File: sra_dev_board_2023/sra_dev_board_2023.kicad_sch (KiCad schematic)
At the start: 75 parts, among them J1 Conn_01x19_Male, J10 Conn_01x03_Male, J11 Conn_01x05_Male, J12 Conn_01x05_Male, J13 Conn_01x05_Male, J14 Conn_01x03_Male, J15 Conn_01x03_Male, J16 Screw_Terminal_01x05, J17 Conn_01x06_Male, J2 Conn_01x03_Male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

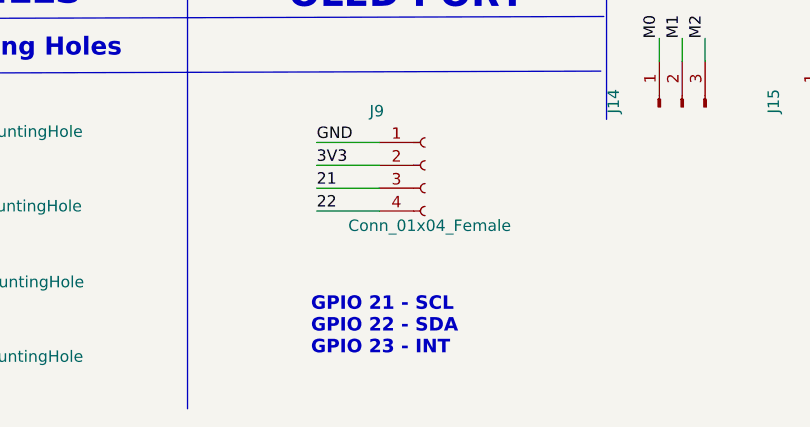
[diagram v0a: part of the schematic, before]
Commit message: Tweaks in routing prototype-1
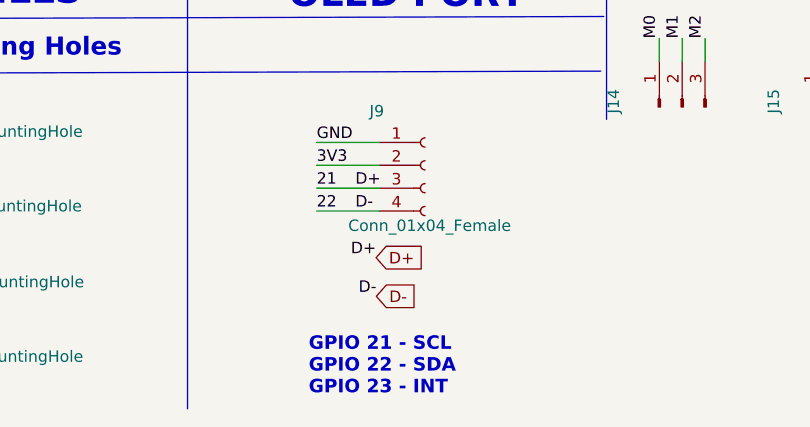
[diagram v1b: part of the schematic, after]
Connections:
- net 21 renamed D+
- net 22 renamed D-
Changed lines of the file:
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@@
     (effects (font (size 3 3) (thickness 0.6) bold) (justify left bottom))
   )
-  (text "GPIO 21 - SCL\nGPIO 22 - SDA\nGPIO 23 - INT\n" (at 144.1704 242.316 0)
+  (text "GPIO 21 - SCL\nGPIO 22 - SDA\nGPIO 23 - INT\n" (at 143.9164 246.761 0)
     (effects (font (size 1.5 1.5) bold) (justify left bottom))
   )
@@
     (effects (font (size 1.27 1.27)) (justify left bottom))
   )
+  (label "D-" (at 151.4348 235.6612 180)
+    (effects (font (size 1.27 1.27)) (justify right bottom))
+  )
   (label "33" (at 26.1366 48.006 0)
     (effects (font (size 1.27 1.27)) (justify left bottom))
@@
     (effects (font (size 1.27 1.27)) (justify right bottom))
   )
+  (label "D+" (at 149.098 223.647 0)
+    (effects (font (size 1.27 1.27)) (justify left bottom))
+  )
   (label "AMS_IN" (at 91.6178 152.908 180)
     (effects (font (size 1.27 1.27)) (justify right bottom))
@@
     (effects (font (size 1.27 1.27)) (justify right bottom))
   )
+  (label "D+" (at 151.4094 231.3686 180)
+    (effects (font (size 1.27 1.27)) (justify right bottom))
+  )
   (label "3V3" (at 200.66 85.09 90)
     (effects (font (size 1.27 1.27)) (justify left bottom))
@@
     (effects (font (size 1.27 1.27)) (justify left bottom))
   )
+  (label "D-" (at 149.098 226.187 0)
+    (effects (font (size 1.27 1.27)) (justify left bottom))
+  )
   (label "3V3" (at 238.76 191.77 0)
     (effects (font (size 1.27 1.27)) (justify left bottom))
@@
     (effects (font (size 1.27 1.27)) (justify left bottom))
   )
+  (global_label "D-" (shape input) (at 151.4348 235.6612 0) (fields_autoplaced)
+    (effects (font (size 1.27 1.27)) (justify left))
+    (property "Intersheet References" "${INTERSHEET_REFS}" (id 0) (at 156.6903 235.5818 0)
+      (effects (font (size 1.27 1.27)) (justify left) hide)
+    )
+  )
+  (global_label "D+" (shape input) (at 151.4094 231.3686 0) (fields_autoplaced)
+    (effects (font (size 1.27 1.27)) (justify left))
+    (property "Intersheet References" "${INTERSHEET_REFS}" (id 0) (at 156.6649 231.2892 0)
+      (effects (font (size 1.27 1.27)) (justify left) hide)
+    )
+  )
   (symbol (lib_id "Device:R") (at 37.8206 175.1838 0) (unit 1)

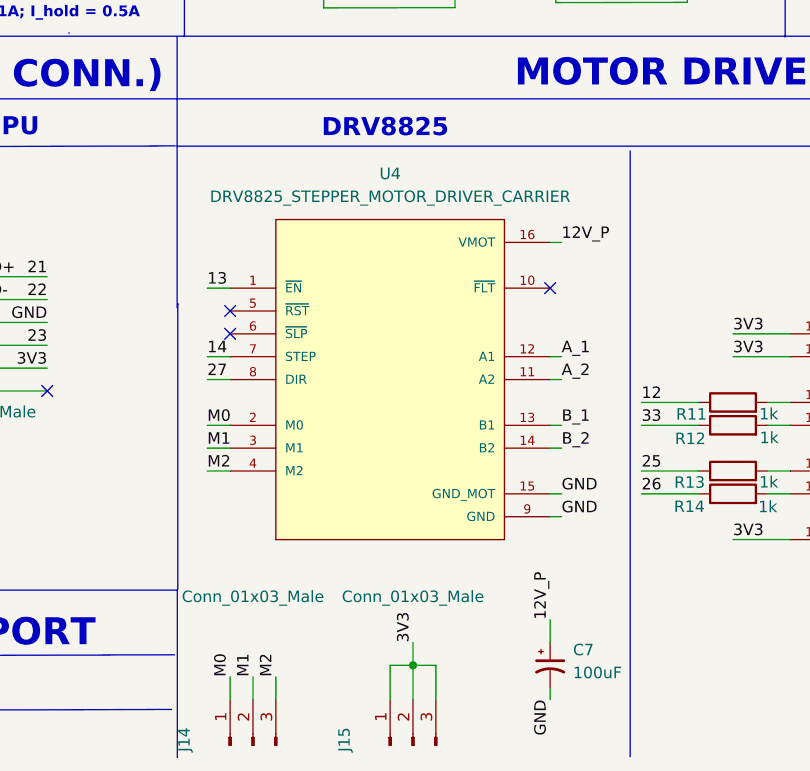
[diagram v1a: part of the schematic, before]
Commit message: Update LSA and SRA board after hardware testing
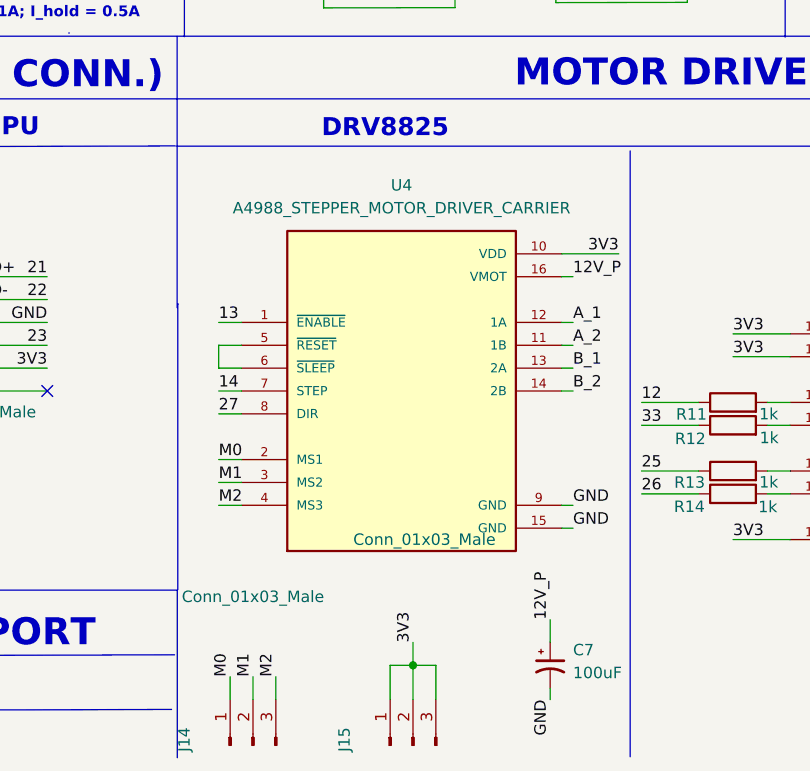
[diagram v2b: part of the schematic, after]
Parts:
- removed U4: DRV8825_STEPPER_MOTOR_DRIVER_CARRIER, stepper_motor_driver:IC_DRV8825_STEPPER_MOTOR_DRIVER_CARRIER, symbol DRV8825_STEPPER_MOTOR_DRIVER_CARRIER:DRV8825_STEPPER_MOTOR_DRIVER_CARRIER
- added U4: A4988_STEPPER_MOTOR_DRIVER_CARRIER, stepper_motor_driver:MODULE_A4988_STEPPER_MOTOR_DRIVER_CARRIER, symbol A4988_STEPPER_MOTOR_DRIVER_CARRIER:A4988_STEPPER_MOTOR_DRIVER_CARRIER
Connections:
- net 12V_P: now also U4.16 (VMOT)
- net 13: now also U4.1 (~{ENABLE})
- net 14: now also U4.7 (STEP)
- net 27: now also U4.8 (DIR)
- net 3V3: now also U4.10 (VDD)
- net A_1: now also U4.12 (1A)
- net A_2: now also U4.11 (1B)
- net B_1: now also U4.13 (2A)
- net B_2: now also U4.14 (2B)
- net GND: now also U4.15 (GND), U4.9 (GND)
- net M0: now also U4.2 (MS1)
- net M1: now also U4.3 (MS2)
- net M2: now also U4.4 (MS3)
- new net: U4.5 (~{RESET}), U4.6 (~{SLEEP})
- no-connect marks 12 -> 9

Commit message: Update repo with recent changes
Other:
- note added: "A4988"
- note removed: "DRV8825"
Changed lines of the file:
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@@
     (effects (font (size 3 3) (thickness 0.6) bold) (justify left bottom))
   )
-  (text "DRV8825" (at 193.04 147.32 0)
+  (text "A4988\n" (at 193.04 147.32 0)
     (effects (font (size 2 2) (thickness 0.6) bold) (justify left bottom))
   )

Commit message: Modify relative path for TCRT5000 footprint
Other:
- note added: "SRA DEVELOPMENT BOARD - 2023"
- note removed: "SRA DEVELOPMENT BOARD - 2022"
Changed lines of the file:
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@@
     (effects (font (size 2 2) (thickness 0.6) bold) (justify left bottom))
   )
-  (text "SRA DEVELOPMENT BOARD - 2022" (at 84.2772 9.8044 0)
+  (text "SRA DEVELOPMENT BOARD - 2023" (at 84.2772 9.8044 0)
     (effects (font (size 5 5) (thickness 1) bold) (justify left bottom))
   )

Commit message: Add current limiting resistor for MPU (#26)
* Add current limiting resistor on Interrupt line for MPU

* Update gerbers, placement files and BoM
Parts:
- added R15: 4.7k, Resistor_SMD:R_0603_1608Metric, symbol Device:R
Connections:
- net 23: now also R15.2; no longer J8.4 (Pin_4)
- new net: J8.4 (Pin_4), R15.1
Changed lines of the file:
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@@
     (stroke (width 0) (type default) (color 0 0 0 0))
   )
+  (wire (pts (xy 173.99 170.18) (xy 170.18 170.18))
+    (stroke (width 0) (type default) (color 0 0 0 0))
+  )
   (wire (pts (xy 151.765 226.187) (xy 144.8054 226.187))
     (stroke (width 0) (type default) (color 0 0 0 0))
@@
     (effects (font (size 1.27 1.27)) (justify left bottom))
   )
-  (label "23" (at 162.56 170.18 180)
+  (label "23" (at 173.99 170.18 180)
     (effects (font (size 1.27 1.27)) (justify right bottom))
   )
@@
     )
   )
+  (symbol (lib_id "Device:R") (at 166.37 170.18 90) (unit 1)
+    (in_bom yes) (on_board yes)
+    (property "Reference" "R15" (id 0) (at 166.37 167.64 90))
+    (property "Value" "4.7k" (id 1) (at 166.37 170.18 90))
+    (property "Footprint" "Resistor_SMD:R_0603_1608Metric" (id 2) (at 166.37 171.958 90)
+      (effects (font (size 1.27 1.27)) hide)
+    )
+    (property "Datasheet" "~" (id 3) (at 166.37 170.18 0)
+      (effects (font (size 1.27 1.27)) hide)
+    )
+    (pin "1")
+    (pin "2")
+  )
   (symbol (lib_id "Connector:Screw_Terminal_01x05") (at 246.38 33.02 0) (unit 1)
     (in_bom yes) (on_board yes) (fields_autoplaced)
@@
       (reference "R14") (unit 1) (value "1k") (footprint "Resistor_SMD:R_1206_3216Metric")
     )
+    (path "/370df534-b389-4320-b330-d64e20c612a4"
+      (reference "R15") (unit 1) (value "4.7k") (footprint "Resistor_SMD:R_0603_1608Metric")
+    )
     (path "/77bcabc8-1188-4d31-8dd6-5a41ab350454"
